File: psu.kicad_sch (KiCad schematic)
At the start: 17 parts, among them J1 HRO_TYPE-C-31-M-12, J2 Battery, J99 Net tie, SW1 Battery, U2 nPM1100-QDAx, U3 TPS22919DCKR

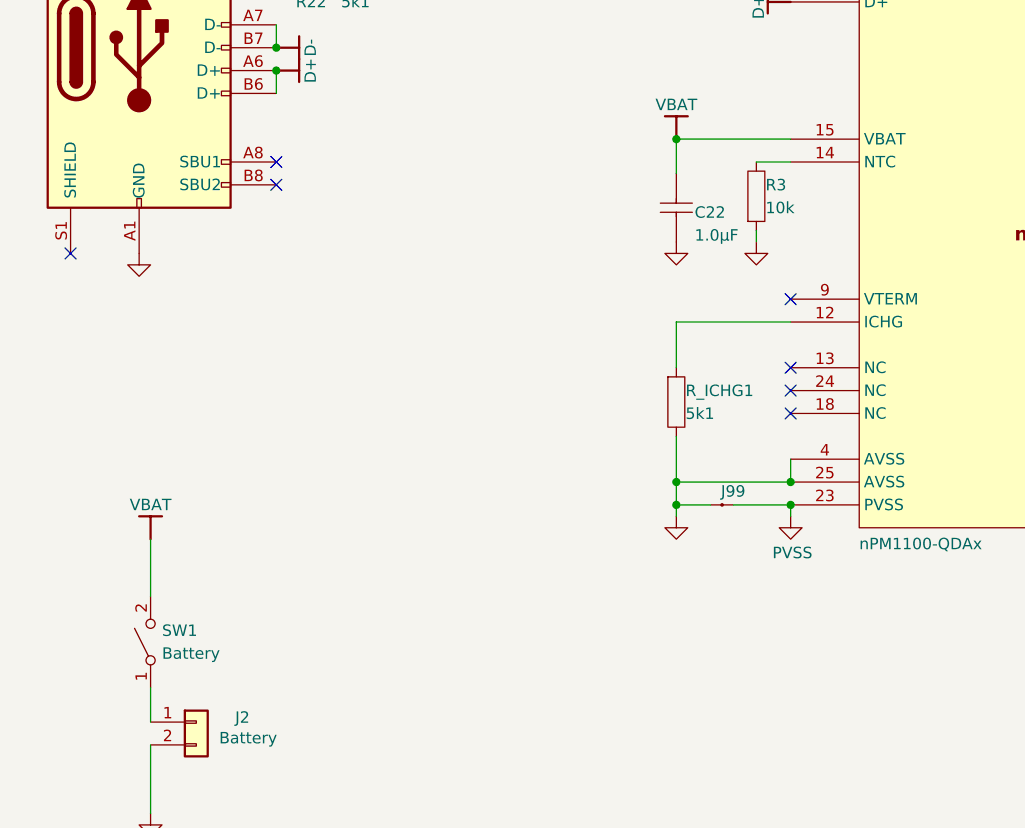
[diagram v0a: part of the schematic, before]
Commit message: Further optimising the BOM and adding JLCPCB specific part numbers
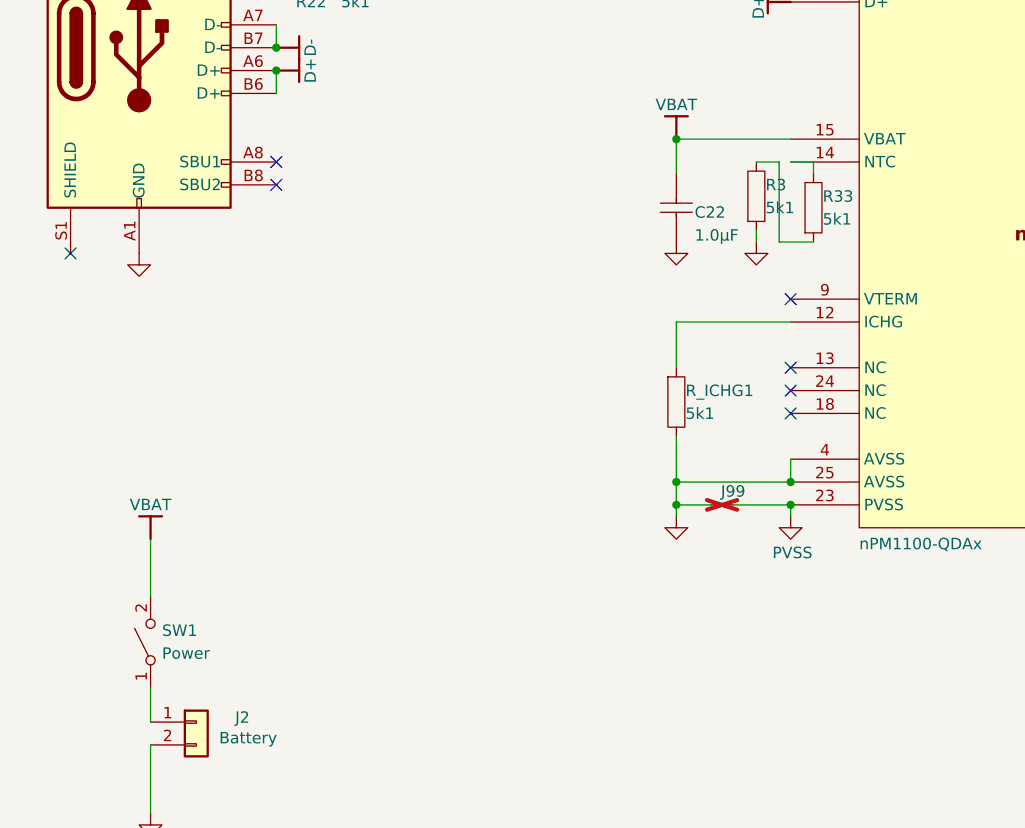
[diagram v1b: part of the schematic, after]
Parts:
- added R33: 5k1, Library:R_0402_1005, symbol AltiumLib:root_3_mirrored_RES_AltiumLib.DbLib
- C22: LCSC (none) -> C52923
- C25, C26: LCSC (none) -> C19702
- J1: LCSC (none) -> C165948
- J2: LCSC (none) -> C160402
- J99: now not fitted
- L5: LCSC (none) -> C1033
- LD2: LCSC (none) -> C84269
- R21, R22, R_ICHG1: LCSC (none) -> C25905
- R3: value 10k -> 5k1; LCSC (none) -> C25905
- R_DIV1, R_DIV2: LCSC (none) -> C25741
- SW1: value Battery -> Power; LCSC (none) -> C431540
- U2: LCSC (none) -> C5816773
- U3: LCSC (none) -> C2149796
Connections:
- net at U2.14 (NTC): now also R33.1; no longer R3.1
- new net: R3.1, R33.2

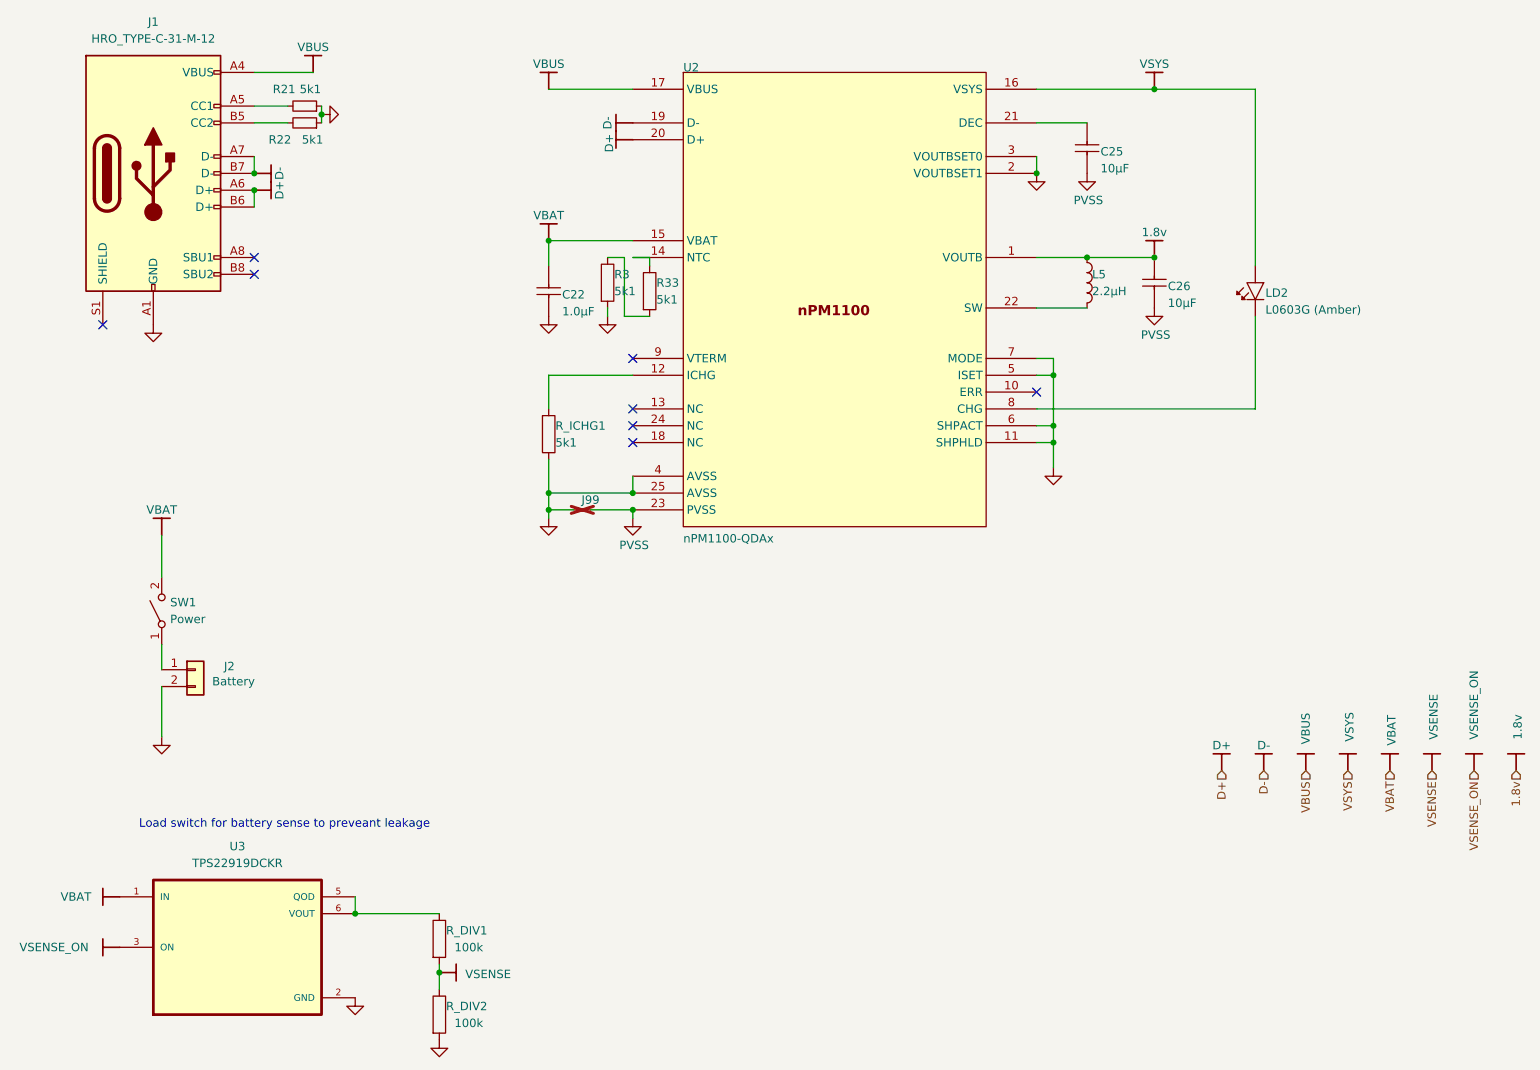
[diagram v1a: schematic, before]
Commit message: Removing the 1.8v power supply option
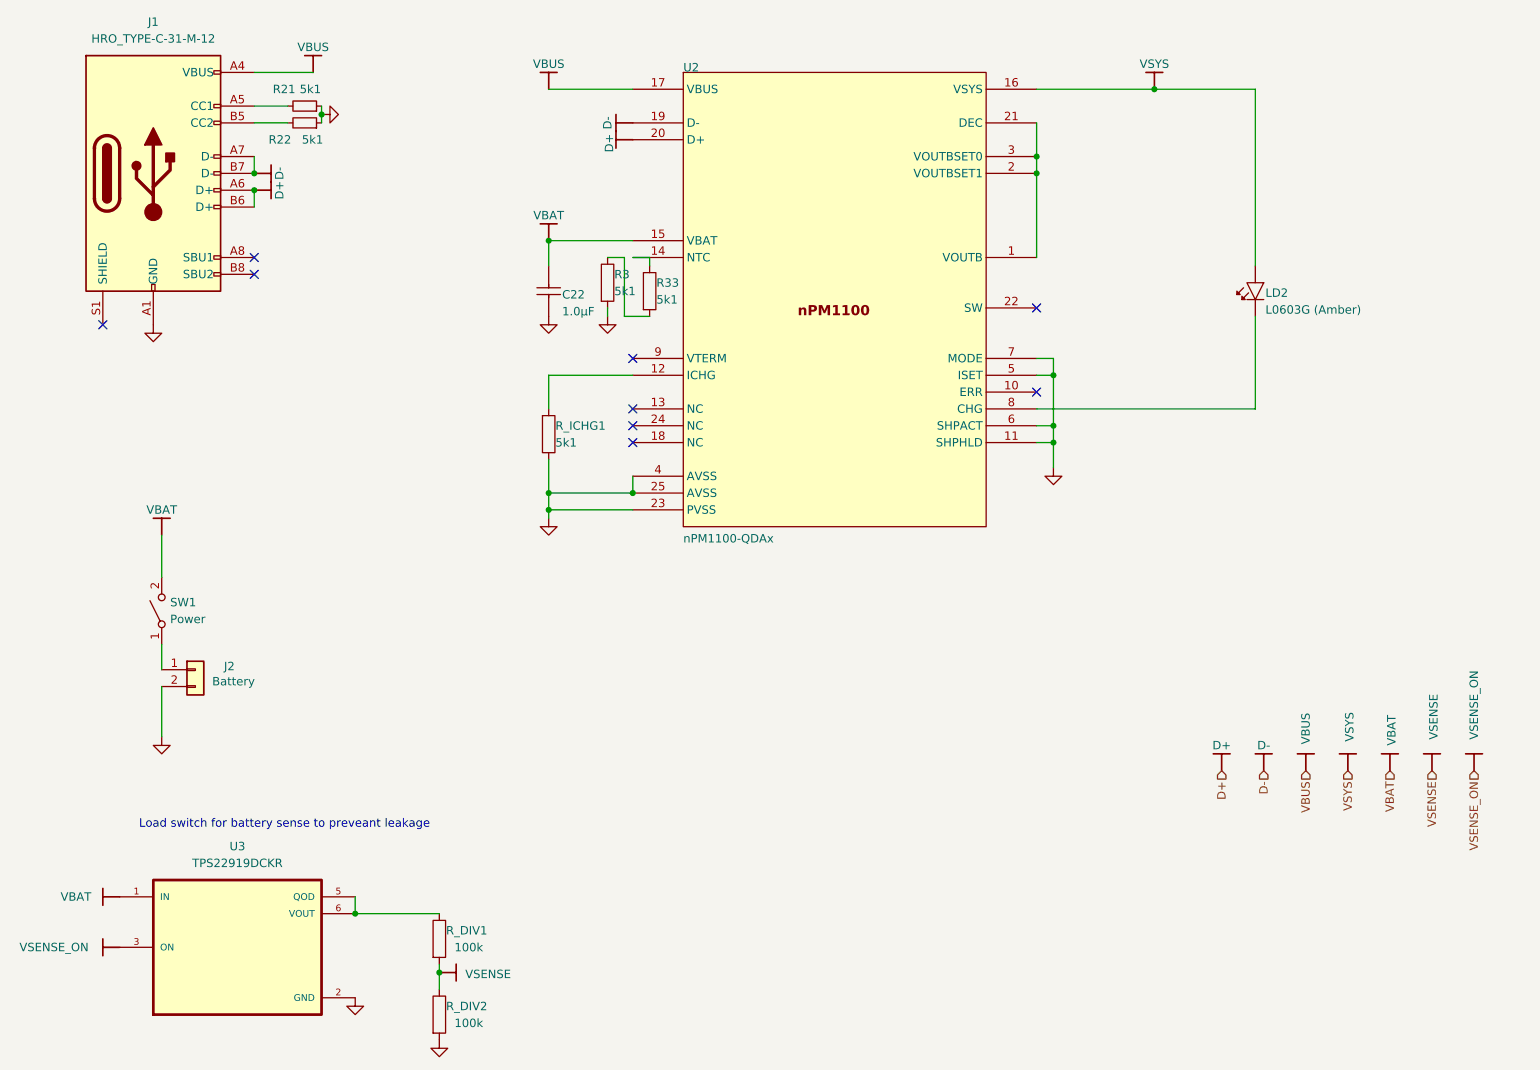
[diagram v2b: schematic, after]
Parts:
- removed C25, C26: 10µF, Library:C_0603_1608, symbol AltiumLib:root_1_CAP_AltiumLib.DbLib
- removed J99: Net tie, 2 pin starpoint:2 PIN STARPOINT, symbol AltiumLib:root_2_mirrored_2 pin starpoint_AltiumLib.DbLib
- removed L5: 2.2µH, Library:L_0603_1608, symbol AltiumLib:root_3_IND_AltiumLib.DbLib
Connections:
- net 1.8v is gone; now on an unnamed net: U2.1 (VOUTB)
- net PVSS is gone; now on net GND: U2.23 (PVSS)
- net GND: no longer U2.2 (VOUTBSET1), U2.3 (VOUTBSET0)
- net at U2.21 (DEC): now also U2.2 (VOUTBSET1), U2.3 (VOUTBSET0)
- no-connect marks 8 -> 9
